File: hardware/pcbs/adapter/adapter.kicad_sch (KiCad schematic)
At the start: 2 parts, among them J1 Conn_01x04_Pin, J2 XLR4

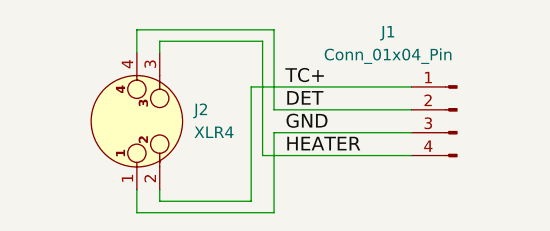
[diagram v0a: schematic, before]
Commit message: feat: update to 5-pin XLR for sleep
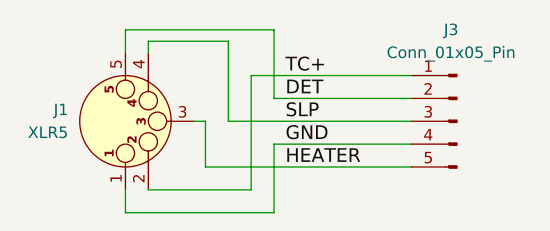
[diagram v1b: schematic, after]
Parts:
- removed J1: Conn_01x04_Pin, Connector_PinHeader_2.54mm:PinHeader_1x04_P2.54mm_Vertical, symbol Connector:Conn_01x04_Pin
- removed J2: XLR4, connector_audio:MiniXLR-4_Rean_RT4MPR, symbol Connector_Audio:XLR4
- added J1: XLR5, connector_audio:MiniXLR-5_Rean_RT5MPR, symbol Connector_Audio:XLR5
- added J3: Conn_01x05_Pin, Connector_PinHeader_2.54mm:PinHeader_1x05_P2.54mm_Vertical, symbol Connector:Conn_01x05_Pin
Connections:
- net DET: now also J1.5 (P5), J3.2 (Pin_2)
- net GND: now also J1.1 (P1), J3.4 (Pin_4)
- net HEATER: now also J1.3 (P3), J3.5 (Pin_5)
- net TC+: now also J1.2 (P2), J3.1 (Pin_1)
- new net SLP: J1.4 (P3), J3.3 (Pin_3)

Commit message: feat: hw v7a
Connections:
- net GND renamed BLUE
- net HEATER renamed RED
- net SLP renamed GREEN
- net TC+ renamed SLP_EXT
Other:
- title: MiniXLR adapter -> MiniXLR adapter (main)
